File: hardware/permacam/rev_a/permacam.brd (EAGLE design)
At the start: 27 x 60 mm, 90 parts, among them J1 TC2030-JLINK-NL, Q1 PMDXB950UPEL, Q3 PMDXB950UPEL, Q5 PMDXB950UPEL, Q6 PMDXB950UPEL, U1 AB1815-T3, U10 NRF52840, U2 BQ25505, U3 EKMB1101111, U4 HM01B0-ANA, U7 MAX17222, U8 MAX44009, X1 32MHz, X3 32.768kHz, X4 ABS07-32.768KHZ-7-T

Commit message: clean and orient design blocks
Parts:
- added C17, C18, C19: 0.1uF, passives:0402_CAP
- added C20: 10uF, passives:0603_CAP
- added R5, R6: 1k, passives:0402_RES
- added U5: MCP1810, chips:SOT-23-5
- moved A2 23.0 mm to (2.97, 28.6), turned to 0 degrees
- moved C13 20.1 mm to (6.39, 28.0), turned to 90 degrees
- moved C14 19.5 mm to (10.2, 28.4), turned to 0 degrees
- moved U$2 18.0 mm to (-13.8, 37.5)
- moved C2 16.0 mm to (2.83, 22.0), turned to 270 degrees
- moved C9 15.9 mm to (5.08, 24.0), turned to 180 degrees
- moved L1 15.1 mm to (4.10, 22.5), turned to 0 degrees
- moved C33 15.1 mm to (-12.7, 8.00)
- moved C34 15.1 mm to (-12.7, 13.6)
- moved C7 15.1 mm to (-11.4, 14.1)
- moved TP6 15.1 mm to (-8.64, 14.1)
- moved X4 15.1 mm to (-12.2, 10.8)
- moved C26 15.1 mm to (-10.2, 13.8)
- moved R11 15.1 mm to (-10.4, 8.26)
- moved R12 15.1 mm to (-10.4, 7.11)
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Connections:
- new net !CAM_EN: U5.2
- new net CAM_D0: U10.AD18, U4.17
- new net CAM_D1: U4.18
- new net CAM_D2: U4.19
- new net CAM_D3: U4.20
- new net CAM_INT: U10.V23, U4.1
- new net CAM_SCL: U10.T2
- new net CAM_SDA: R5.2, R6.2, U10.M2, U4.2, U4.3
- new net CAM_TRIG: U10.W24, U4.6
- new net FVLD: U10.AD20, U4.5
- new net LVLD: U10.AC19, U4.4
- new net MCLK: U10.AD16, U4.15
- new net PCLKO: U10.AC17, U4.16
- new net VCC28: C17.1, C18.1, C19.1, C20.1, R5.1, R6.1, U4.12, U4.13, U4.14, U4.23, U4.8, U5.3
- net !LT_EN: now also U10.Y23; no longer U10.AD20
- net GND: now also C17.2, C18.2, C19.2, C20.2, U4.10, U4.11, U4.24, U4.7, U4.9, U5.5
- net VCC: now also U5.1
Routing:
- net !LT_EN: track 23.9 -> 8.31 mm
- net LBST: track 24.3 -> 9.85 mm, vias 3 -> 2
- net !LT_INT: track 20.3 -> 7.52 mm
- net VSEC: track 32.4 -> 19.8 mm
- net VBAT_OK: track 13.6 -> 1.05 mm
- net !RST: track 36.0 -> 25.1 mm
- net !PIR_EN: track 12.1 -> 1.32 mm
- net SWDCLK: track 15.7 -> 5.34 mm
- net SWDIO: track 13.6 -> 4.31 mm
- net RTC_CS: track 12.9 -> 5.12 mm, vias 3 -> 2
- net LED_GREEN: track 17.6 -> 12.7 mm
- net LED_BLUE: track 16.7 -> 12.1 mm
- net LED_RED: track 14.3 -> 10.2 mm
- net PIR_OUT: track 14.9 -> 12.0 mm
- net !RTC_IRQ2: track 12.9 -> 10.7 mm, vias 2 -> 1
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
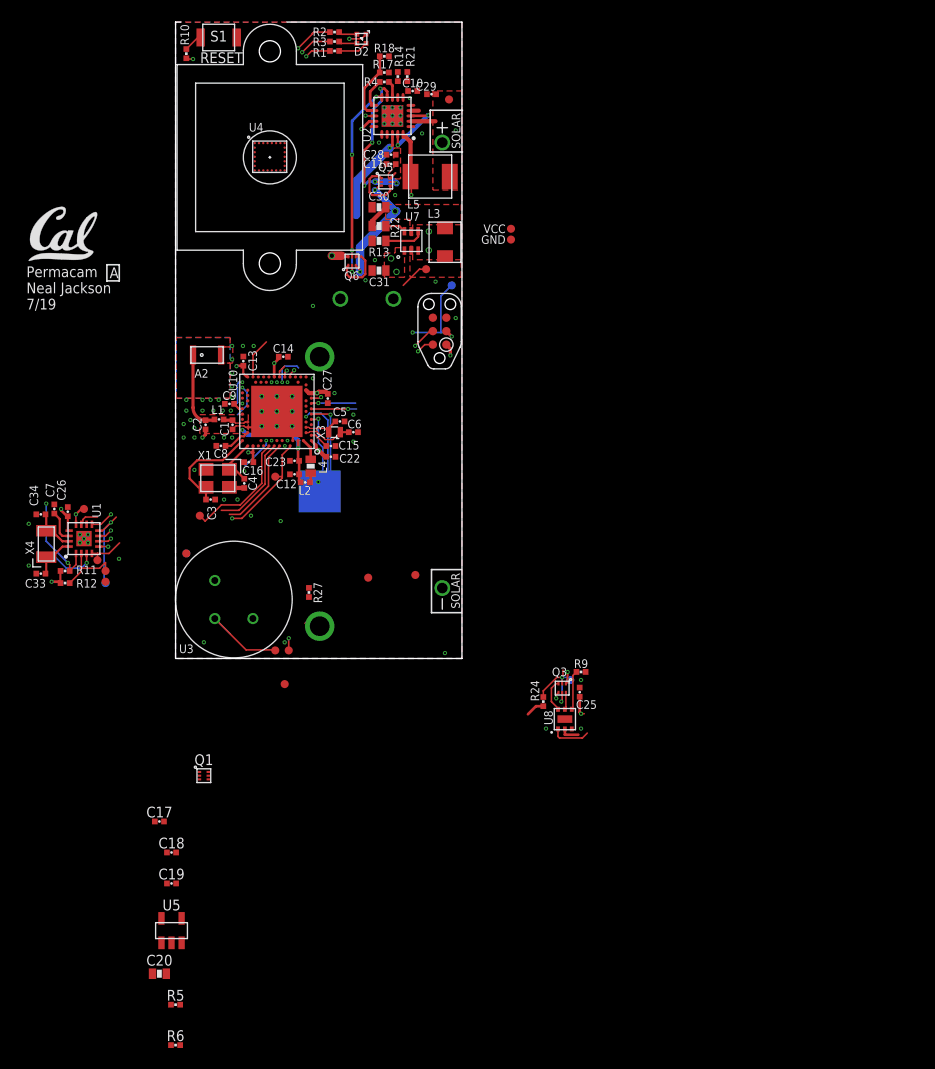
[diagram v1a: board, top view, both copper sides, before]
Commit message: Route signals on board - no airwires or major drc
Need to add optional MSP430
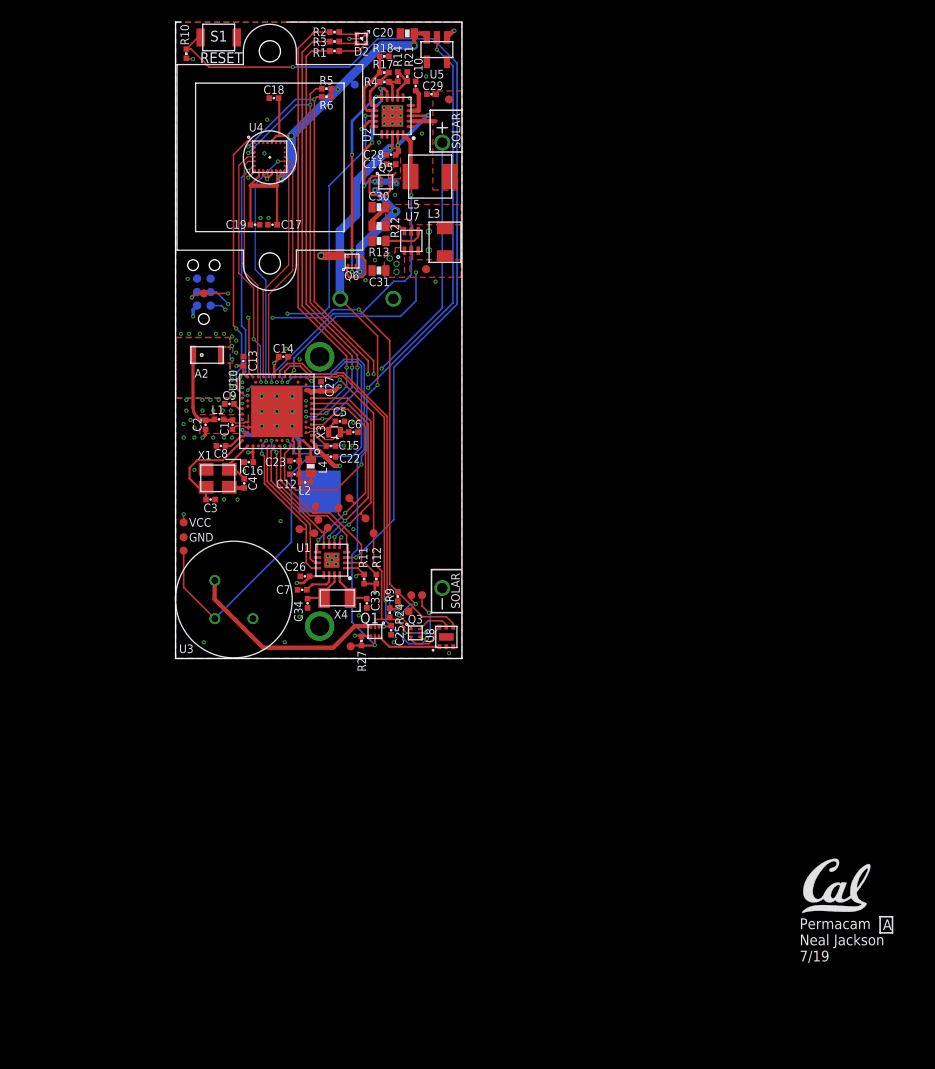
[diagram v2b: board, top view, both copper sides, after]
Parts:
- removed TP24: TEST-POINT, headers:PAD.03X.03
- added TP7: TEST-POINT, headers:PAD.03X.03
- moved U$2 95.4 mm to (59.1, -24.0)
- moved C20 91.7 mm to (21.8, 58.9), turned to 180 degrees
- moved R6 90.5 mm to (14.2, 53.0), turned to 180 degrees
- moved R5 87.5 mm to (14.2, 53.7), turned to 180 degrees
- moved U5 86.7 mm to (24.6, 57.4), turned to 180 degrees
- moved C18 71.8 mm to (9.27, 52.8), turned to 180 degrees
- moved C19 62.6 mm to (7.49, 40.9)
- moved C17 57.3 mm to (9.14, 40.9), turned to 180 degrees
- moved TP27 41.7 mm to (0.76, 11.4)
- moved TP26 41.5 mm to (0.76, 12.8)
- moved C33 30.9 mm to (18.0, 5.21), turned to 270 degrees
- moved R12 29.3 mm to (18.9, 7.49), turned to 270 degrees
- moved TP2 28.9 mm to (22.2, 5.97), turned to 0 degrees
- moved R11 28.2 mm to (17.8, 7.49), turned to 270 degrees
- moved X4 27.9 mm to (15.2, 5.71), turned to 180 degrees
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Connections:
- removed net !PR_EN: U10.B19
- net !CAM_EN: now also U10.G1
- net !PIR_EN: now also U10.AC11; no longer U10.AD12
- net CAM_D0: now also U10.AD16; no longer U10.AD18
- net CAM_SCL: now also R5.2, U4.3
- net CAM_SDA: no longer R5.2, U4.3
- net LED_BLUE: now also U10.L1; no longer U10.K2
- net LED_GREEN: now also U10.K2; no longer U10.L1
- net MCLK: now also U10.AD18; no longer U10.AD16
- net MISO: now also U10.U1; no longer U10.R1
- net PIR_OUT: now also U10.AC9; no longer U10.AC11
- net SCK: now also U10.R1; no longer U10.U1
- net SCL: now also U10.AD12; no longer U10.AC9
- net VCC28: now also TP7.P$1
- net VSEC: no longer TP24.P$1
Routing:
- net !RTC_EXTR: track 6.78 -> 81.5 mm, vias 1 -> 2
- net CAM_SDA: track 0.00 -> 45.6 mm, vias 0 -> 4
- net VCC28: track 0.00 -> 45.6 mm, vias 0 -> 4
- net CAM_SCL: track 0.00 -> 45.4 mm, vias 0 -> 4
- net !LT_INT: track 7.52 -> 52.0 mm, vias 0 -> 3
- net !CAM_EN: track 0.00 -> 43.8 mm, vias 0 -> 3
- net SDA: track 1.32 -> 41.7 mm, vias 2 -> 3
- net !PIR_EN: track 1.32 -> 40.0 mm, vias 0 -> 2
- net PIR_OUT: track 12.0 -> 47.5 mm
- net VBAT_OK: track 1.05 -> 34.9 mm, vias 2 -> 3
- net VSOL: track 7.82 -> 41.2 mm, vias 1 -> 3
- net !LT_EN: track 8.31 -> 41.2 mm, vias 2 -> 4
- net LED_RED: track 10.2 -> 41.4 mm
- net LED_GREEN: track 12.7 -> 42.4 mm
- net LED_BLUE: track 12.1 -> 41.5 mm
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
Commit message: Rearrange pin assignments to match board locations
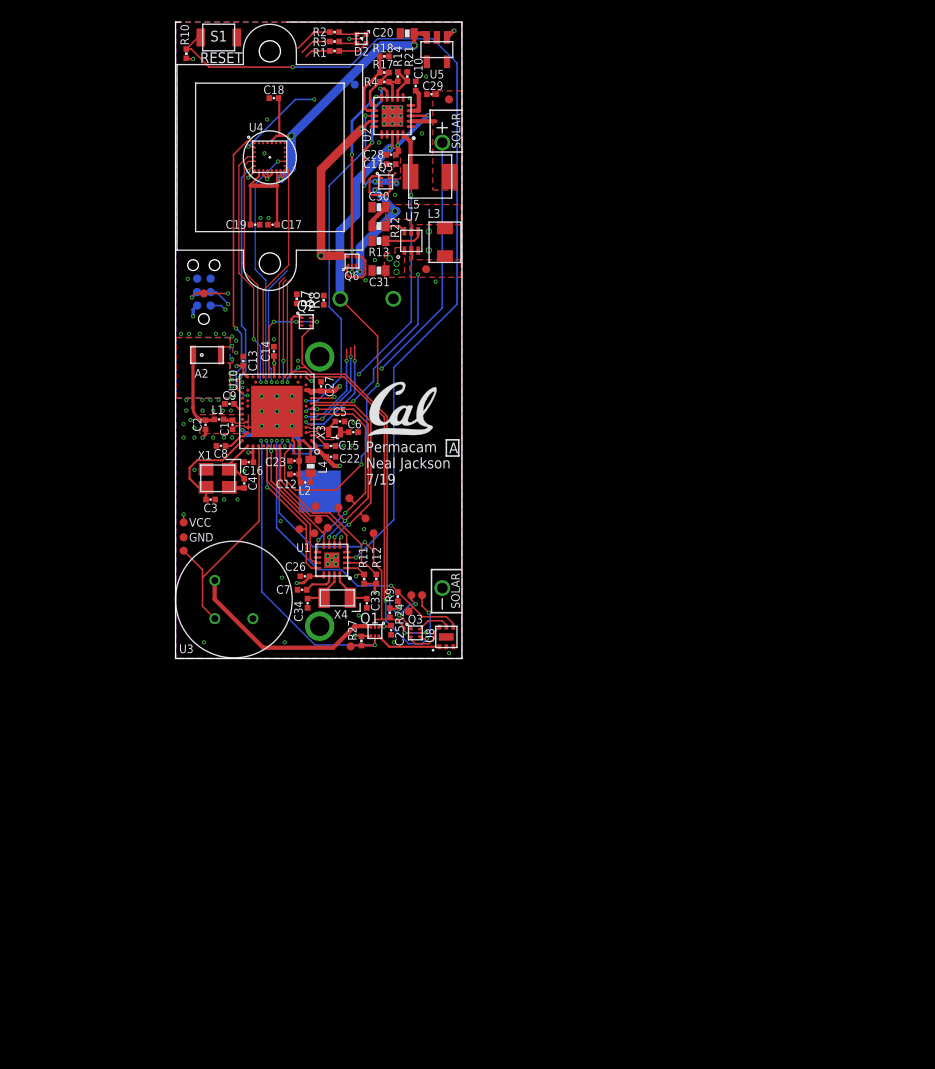
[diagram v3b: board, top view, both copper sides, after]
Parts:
- removed R5, R6: 1k, passives:0402_RES
- added Q2: PMDXB950UPEL, fets:XDFN-6
- added R7, R8: 1k, passives:0402_RES
- moved U$2 60.8 mm to (18.2, 21.0)
- moved C14 1.02 mm to (9.27, 29.0), turned to 90 degrees
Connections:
- net !CAM_EN: now also Q2.2, Q2.5, U10.AD16; no longer U10.G1
- net !LT_EN: now also U10.B11; no longer U10.Y23
- net !LT_INT: now also U10.B13; no longer U10.AD22
- net !PIR_EN: now also U10.B19; no longer U10.AC11
- net !RTC_IRQ2: now also U10.A14; no longer U10.B15
- net !RTC_IRQ3: now also U10.B15; no longer U10.A14
- net CAM_D0: now also U10.AD10; no longer U10.AD16
- net CAM_D1: now also U10.AC11
- net CAM_D2: now also U10.AD12
- net CAM_D3: now also U10.AC15
- net CAM_SCL: now also Q2.3; no longer R5.2, U10.T2
- net CAM_SDA: now also Q2.6; no longer R6.2, U10.M2
- net LBST: now also U10.U1; no longer U10.AC15
- net LED_BLUE: now also U10.J1; no longer U10.L1
- net LED_RED: now also U10.H2; no longer U10.J1
- net MISO: now also U10.N1; no longer U10.U1
- net MOSI: now also U10.L1; no longer U10.N1
- net PIR_OUT: now also U10.A20; no longer U10.AC9
- net SCK: now also U10.M2; no longer U10.R1
- net SCL: now also Q2.4, R8.1, U10.AC9; no longer U10.AD12
- net SDA: now also Q2.1, R7.1, U10.AD8; no longer U10.AD10
- net SW: now also U10.R1; no longer U10.AD8
- net VBAT_OK: now also U10.T2; no longer U10.R24
- net VCC28: now also R7.2, R8.2; no longer R5.1, R6.1
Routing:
- net CAM_SCL: track 45.4 -> 0.00 mm, vias 4 -> 0
- net CAM_SDA: track 45.6 -> 8.71 mm, vias 4 -> 2
- net !CAM_EN: track 43.8 -> 10.6 mm
- net LED_GREEN: track 42.4 -> 12.4 mm
- net LED_BLUE: track 41.5 -> 11.9 mm
- net LED_RED: track 41.4 -> 12.8 mm
- net PIR_OUT: track 47.5 -> 22.3 mm, vias 1 -> 0
- net !LT_INT: track 52.0 -> 29.5 mm, vias 3 -> 2
- net CAM_D0: track 22.0 -> 9.37 mm
- net CAM_D3: track 0.00 -> 11.4 mm, vias 0 -> 1
- net CAM_D1: track 0.00 -> 9.82 mm, vias 0 -> 2
- net !PIR_EN: track 40.0 -> 30.2 mm
- net CAM_D2: track 0.00 -> 9.62 mm
- net !LT_EN: track 41.2 -> 33.9 mm
- net SDA: track 41.7 -> 46.8 mm
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
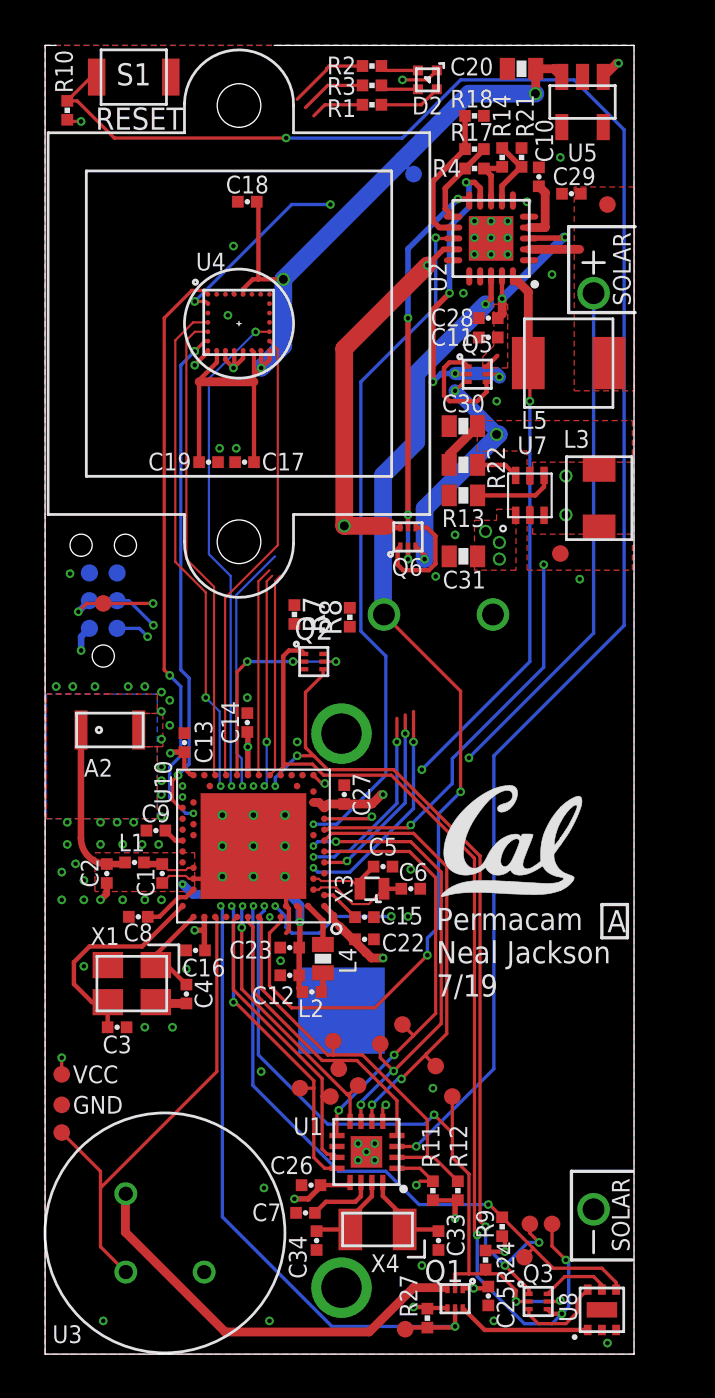
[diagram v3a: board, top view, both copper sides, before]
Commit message: Use serial data + one vcc at 2.8V
Need to divide primary cell voltage for sensing
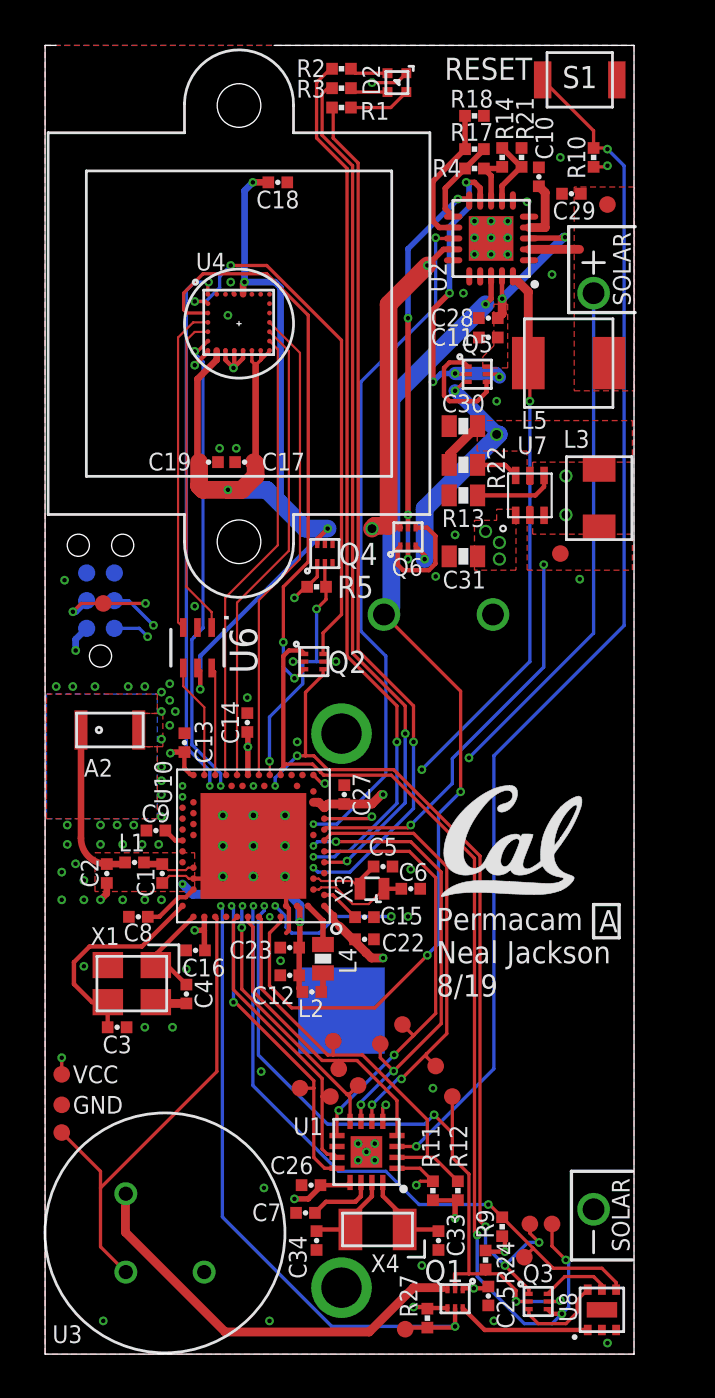
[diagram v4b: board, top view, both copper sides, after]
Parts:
- removed C20: 10uF, passives:0603_CAP
- removed R7, R8: 1k, passives:0402_RES
- removed TP7: TEST-POINT, headers:PAD.03X.03
- removed U5: MCP1810, chips:SOT-23-5
- added Q4: PMDXB950UPEL, fets:XDFN-6
- added R5: 100M, passives:0402_RES
- added U6: SN74AUP2G04DCKRDCK6-L, chips:DCK6-L
- R13: value 80.6k -> 215k
- moved R10 24.2 mm to (25.1, 54.9)
- moved S1 20.4 mm to (24.5, 58.4)
- moved C18 1.66 mm to (10.7, 53.7), turned to 0 degrees
- moved R1 1.40 mm to (13.6, 57.1)
- moved R2 1.40 mm to (13.6, 58.9)
- moved R3 1.40 mm to (13.6, 58.0)
- moved D2 1.40 mm to (16.1, 58.3)
- moved J1 0.13 mm to (2.54, 34.5)
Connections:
- removed net VCC28: C17.1, C18.1, C19.1, C20.1, R7.2, R8.2, TP7.P$1, U4.12, U4.13, U4.14, U4.23, U4.8, U5.3
- new net !FVLD: U4.5, U6.1
- new net !LVLD: U4.4, U6.3
- new net N$16: C17.1, C18.1, C19.1, Q4.6, U4.12, U4.13, U4.14, U4.23, U4.8, U6.5
- net !CAM_EN: now also Q4.2, R5.1, U10.AD10; no longer U10.AD16, U5.2
- net CAM_D0: now also U10.AD12; no longer U10.AD10
- net CAM_D1: no longer U10.AC11
- net CAM_D2: no longer U10.AD12
- net CAM_D3: no longer U10.AC15
- net CAM_INT: now also U10.AC21; no longer U10.V23
- net CAM_TRIG: now also U10.AC19; no longer U10.W24
- net FVLD: now also U6.6; no longer U4.5
- net GND: now also U6.2; no longer C20.2, U5.5
- net LVLD: now also U10.AD22, U6.4; no longer U10.AC19, U4.4
- net PCLKO: now also U10.AD16; no longer U10.AC17
- net SCL: no longer R8.1
- net SDA: no longer R7.1
- net VCC: now also Q4.1, R5.2; no longer U5.1
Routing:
- net N$16: track 0.00 -> 51.6 mm, vias 0 -> 5
- net VCC28: track 44.1 -> 0.00 mm, vias 3 -> 0
- net LED_GREEN: track 12.4 -> 40.4 mm
- net LED_BLUE: track 11.9 -> 39.5 mm
- net LED_RED: track 12.8 -> 39.6 mm
- net CAM_SCL: track 0.00 -> 26.8 mm, vias 0 -> 2
- net !RTC_EXTR: track 81.5 -> 55.9 mm
- net LVLD: track 23.1 -> 5.31 mm, vias 2 -> 0
- net FVLD: track 21.6 -> 4.98 mm
- net CAM_SDA: track 8.71 -> 24.5 mm
- net !LVLD: track 0.00 -> 15.0 mm
- net !FVLD: track 0.00 -> 14.8 mm
- net CAM_D0: track 9.37 -> 22.1 mm
- net CAM_D3: track 11.4 -> 0.00 mm, vias 1 -> 0
- net CAM_D1: track 9.82 -> 0.00 mm, vias 2 -> 0
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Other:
- board text added: "Permacam Neal Jackson 8/19"
- board text removed: "Permacam Neal Jackson 7/19"
